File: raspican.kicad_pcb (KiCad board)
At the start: 2 copper layers, 85 x 56 mm, 1 part, among them P1 CONN_13X2

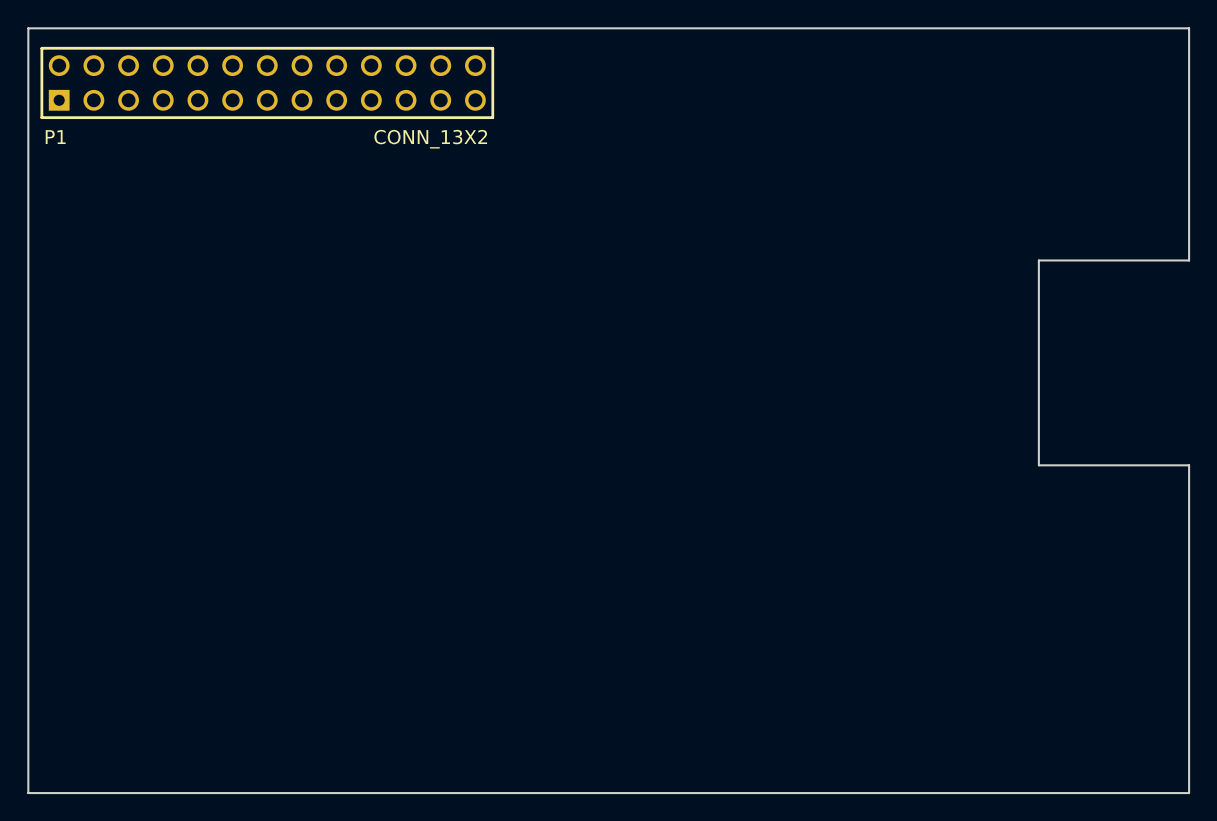
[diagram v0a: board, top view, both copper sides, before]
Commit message: place most parts, fix grid
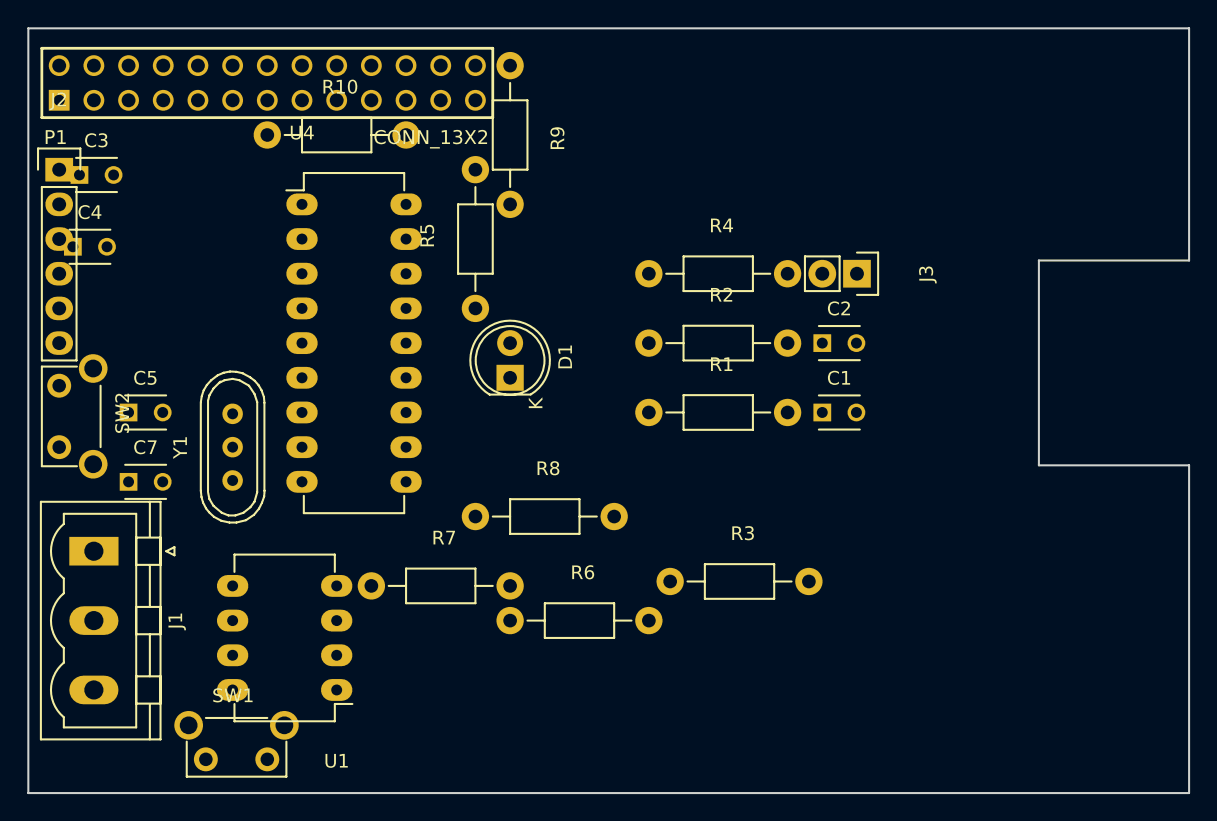
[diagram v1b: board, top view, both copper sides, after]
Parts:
- added C1: 560pF, Capacitors_ThroughHole:C_Disc_D3_P2.5, F.Cu at (201.6, 153.1)
- added C2: 560pF, Capacitors_ThroughHole:C_Disc_D3_P2.5, F.Cu at (201.6, 148.1)
- added C3: 0.1μF, Capacitors_ThroughHole:C_Disc_D3_P2.5, F.Cu at (147.2, 135.7)
- added C4: 0.1μF, Capacitors_ThroughHole:C_Disc_D3_P2.5, F.Cu at (146.8, 141.0)
- added C5: 22pF, Capacitors_ThroughHole:C_Disc_D3_P2.5, F.Cu at (150.8, 153.1)
- added C7: 22pF, Capacitors_ThroughHole:C_Disc_D3_P2.5, F.Cu at (150.8, 158.2)
- added D1: LED, LEDs:LED-5MM, F.Cu at (178.8, 150.6)
- added J1: CANBUS, Connectors_Phoenix:PhoenixContact_MSTBVA-G_03x5.08mm_Vertical, F.Cu at (148.3, 163.3)
- added J2: TTL_SERIAL, Pin_Headers:Pin_Header_Straight_1x06, F.Cu at (145.8, 135.3)
- added J3: TERMINATE, Pin_Headers:Pin_Header_Straight_1x02, F.Cu at (204.2, 143.0)
- added R1: 100Ω, Resistors_ThroughHole:Resistor_Horizontal_RM10mm, F.Cu at (188.9, 153.1)
- added R10: 1KΩ, Resistors_ThroughHole:Resistor_Horizontal_RM10mm, F.Cu at (161.0, 132.8)
- added R2: 100Ω, Resistors_ThroughHole:Resistor_Horizontal_RM10mm, F.Cu at (188.9, 148.1)
- added R3: 4K7Ω, Resistors_ThroughHole:Resistor_Horizontal_RM10mm, F.Cu at (190.5, 165.5)
- added R4: 120Ω, Resistors_ThroughHole:Resistor_Horizontal_RM10mm, F.Cu at (188.9, 143.0)
- added R5: 4K7Ω, Resistors_ThroughHole:Resistor_Horizontal_RM10mm, F.Cu at (176.2, 145.5)
- added R6: 18KΩ, Resistors_ThroughHole:Resistor_Horizontal_RM10mm, F.Cu at (178.8, 168.4)
- added R7: 10KΩ, Resistors_ThroughHole:Resistor_Horizontal_RM10mm, F.Cu at (168.6, 165.8)
- added R8: 1KΩ, Resistors_ThroughHole:Resistor_Horizontal_RM10mm, F.Cu at (176.2, 160.8)
- added R9: 1KΩ, Resistors_ThroughHole:Resistor_Horizontal_RM10mm, F.Cu at (178.8, 127.7)
- added SW1: BUTTON_FRAME, Buttons_Switches_ThroughHole:SW_Tactile_SPST_Angled, F.Cu at (161.0, 178.5)
- added SW2: BUTTON_FRAME, Buttons_Switches_ThroughHole:SW_Tactile_SPST_Angled, F.Cu at (145.8, 155.7)
- added U1: MCP2551-I/P, Housings_DIP:DIP-8_W7.62mm_LongPads, F.Cu at (166.1, 173.4)
- added U4: MCP2515, Housings_DIP:DIP-18_W7.62mm_LongPads, F.Cu at (163.5, 137.9)
- added Y1: 16MHz, Crystals:Crystal_HC49-U_Vertical_3Pin, F.Cu at (158.5, 155.7)
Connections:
- P1 pad 10: (no net) -> /RXD
- P1 pad 11: (no net) -> /GPIO17
- P1 pad 12: (no net) -> /GPIO18
- P1 pad 13: (no net) -> /GPIO21
- P1 pad 14: (no net) -> Net-(P1-Pad14)
- P1 pad 15: (no net) -> /GPIO22
- P1 pad 16: (no net) -> /GPIO23
- P1 pad 17: (no net) -> Net-(P1-Pad17)
- P1 pad 18: (no net) -> /GPIO24
- P1 pad 19: (no net) -> /GPIO10(MOSI)
- P1 pad 20: (no net) -> Net-(P1-Pad20)
- P1 pad 21: (no net) -> /GPIO9(MISO)
- P1 pad 22: (no net) -> /GPIO25
- P1 pad 23: (no net) -> /GPIO11(SCLK)
- P1 pad 24: (no net) -> /GPIO8(CE0)
- P1 pad 25: (no net) -> Net-(P1-Pad25)
- P1 pad 26: (no net) -> /GPIO7(CE1)
- P1 pad 3: (no net) -> /GPIO0(SDA)
- P1 pad 4: (no net) -> Net-(P1-Pad4)
- P1 pad 5: (no net) -> /GPIO1(SCL)
- P1 pad 7: (no net) -> /GPIO4
- P1 pad 8: (no net) -> /TXD
- P1 pad 9: (no net) -> Net-(P1-Pad9)
